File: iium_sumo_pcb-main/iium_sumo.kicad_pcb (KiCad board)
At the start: 2 copper layers, 101.3 x 62.2 mm, 58 parts, among them J12 Conn_01x04, J14 Conn_01x04, J15 EXTRA1, J16 Conn_01x02_Pin, J17 Conn_01x02_Pin, SW1 SW_SPST, SW2 SW_SPST, U1 TPS54360DDA, U4 Black Pill v2, U5 LM3940

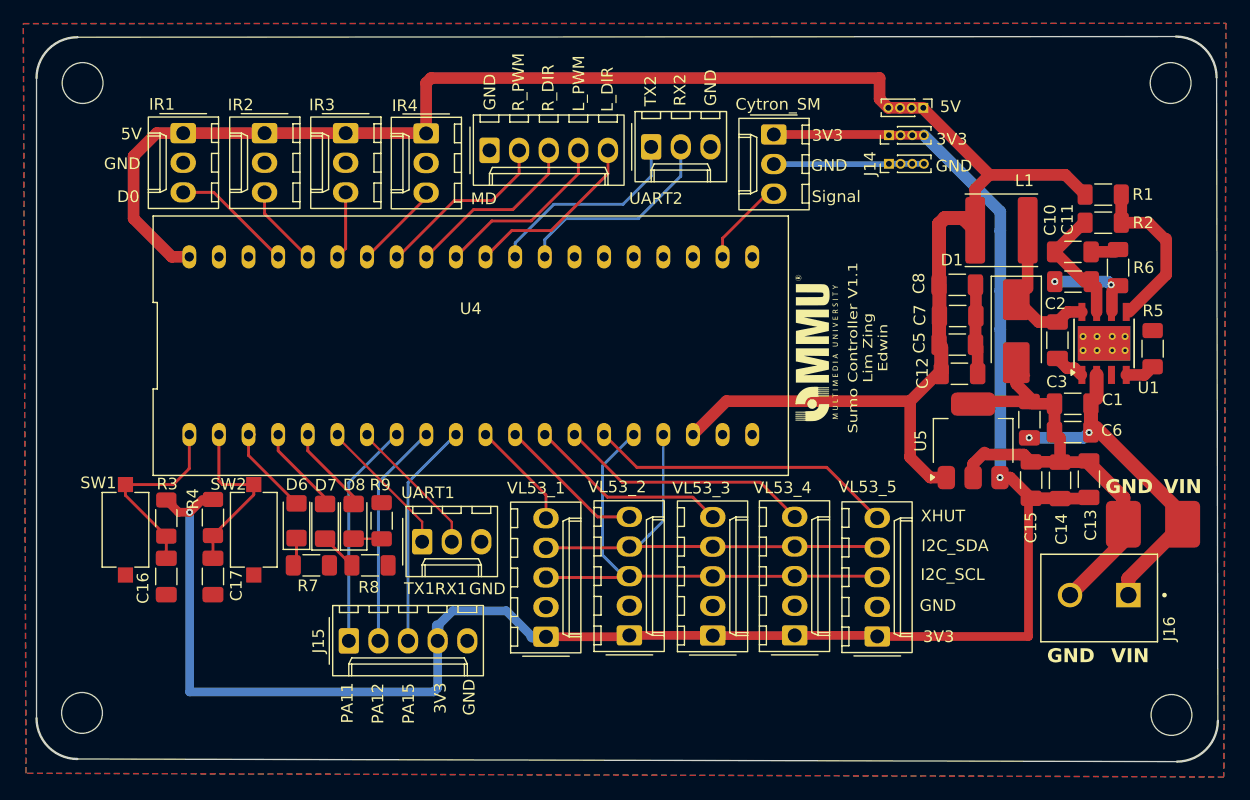
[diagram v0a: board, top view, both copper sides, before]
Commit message: Added Labels
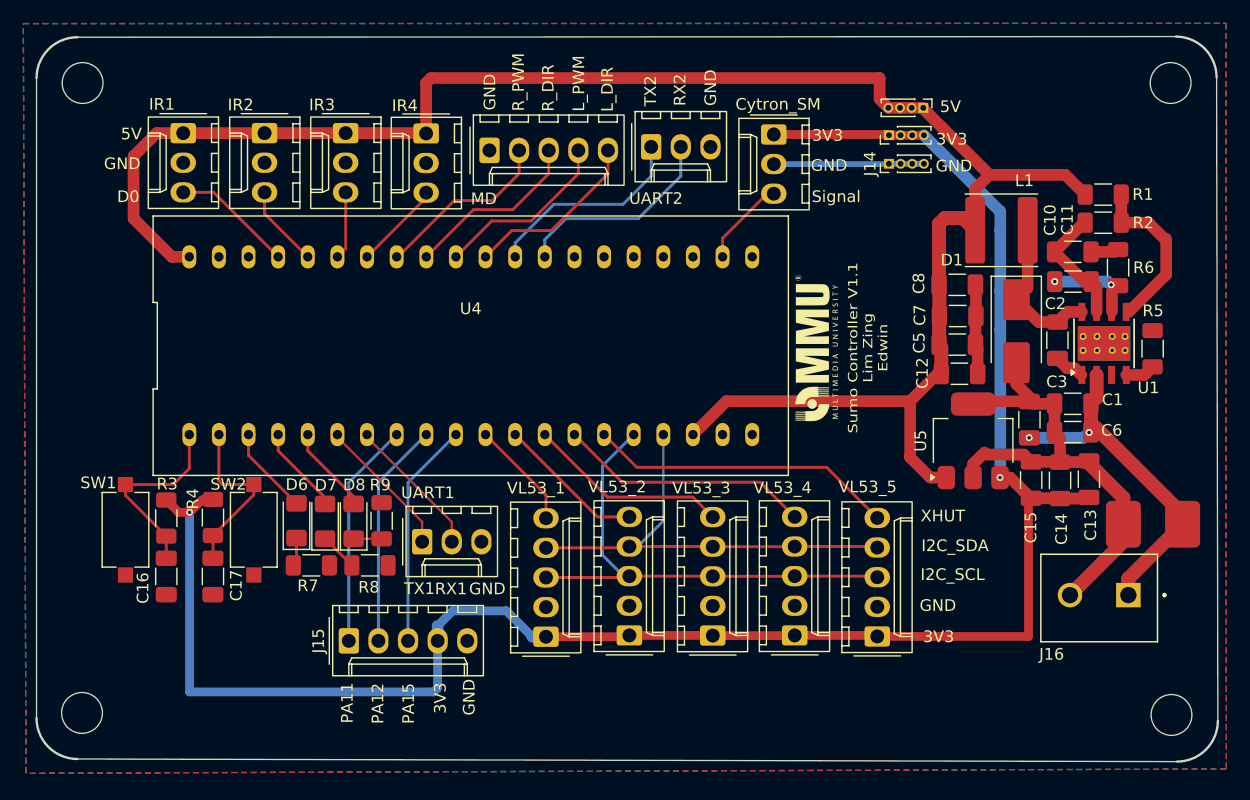
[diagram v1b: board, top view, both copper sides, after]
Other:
- board text removed: "VIN"
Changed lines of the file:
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@@
 		(at 187.475 108.1 180)
 		(property "Reference" "J16"
-			(at -6.025 -2.9 270)
+			(at 4.075 -5.075 0)
 			(layer "F.SilkS")
 			(effects
@@
 		)
 	)
-	(gr_text "GND"
-		(at 183 114 0)
-		(layer "F.SilkS")
-		(effects
-			(font
-				(size 1.2 1.2)
-				(thickness 0.3)
-				(bold yes)
-			)
-			(justify left bottom)
-		)
-	)
-	(gr_text "GND"
-		(at 188 99.5 0)
-		(layer "F.SilkS")
-		(effects
-			(font
-				(size 1.2 1.2)
-				(thickness 0.3)
-				(bold yes)
-			)
-			(justify left bottom)
-		)
-	)
-	(gr_text "VIN"
-		(at 188.5 114 0)
-		(layer "F.SilkS")
-		(effects
-			(font
-				(size 1.2 1.2)
-				(thickness 0.3)
-				(bold yes)
-			)
-			(justify left bottom)
-		)
-	)
-	(gr_text "VIN"
-		(at 193 99.5 0)
-		(layer "F.SilkS")
-		(effects
-			(font
-				(size 1.2 1.2)
-				(thickness 0.3)
-				(bold yes)
-			)
-			(justify left bottom)
-		)
-	)
 	(segment
 		(start 159.58 68.61)
@@
 		(polygon
 			(pts
-				(xy 95.244021 59.105209) (xy 198.355042 59.08266) (xy 198.157327 123.689238) (xy 95.475 123.375)
+				(xy 95.244021 59.105209) (xy 198.355042 59.08266) (xy 198.369021 123.005209) (xy 95.475 123.375)
 			)
 		)
